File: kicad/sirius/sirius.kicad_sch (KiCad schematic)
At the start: 58 parts, among them J1 IPEX_MHF1, J2 Power In, J3 Screw_Terminal, Q1 Q_PMOS_GSD, Q2 Q_NMOS_GSD, Q3 Q_NMOS_GSD, U1 Power_Connector, U2 AP63301WU-7, U3 RFM95W-915S2, U4 LC29H (DA), U5 Pi Zero 2W

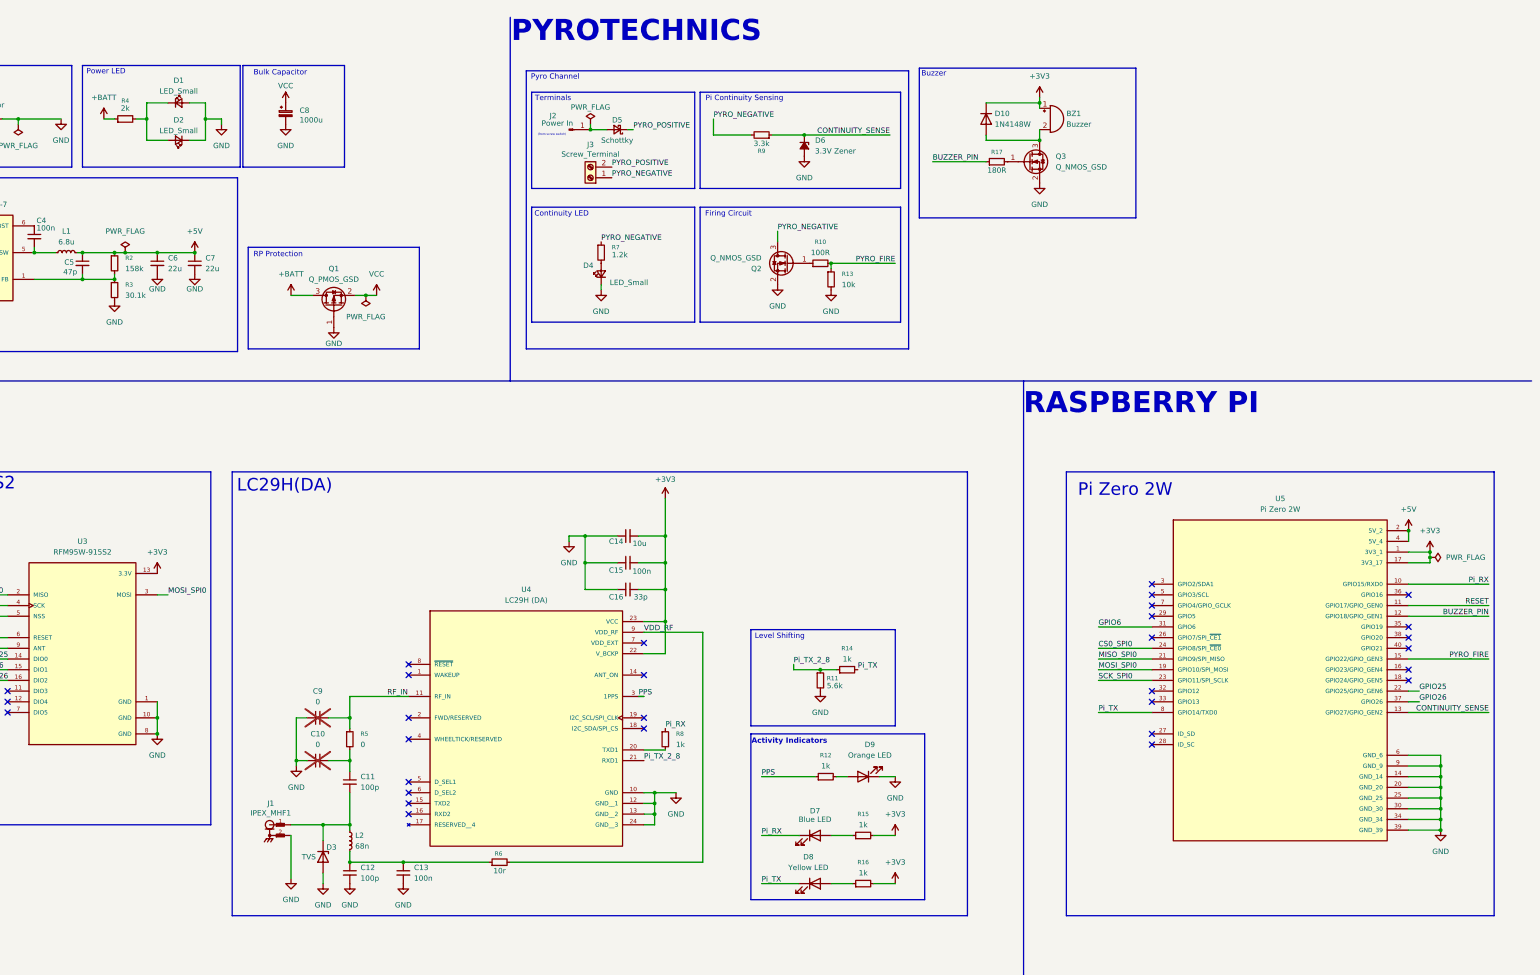
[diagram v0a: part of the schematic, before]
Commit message: WIP: Start making new version of Sirius
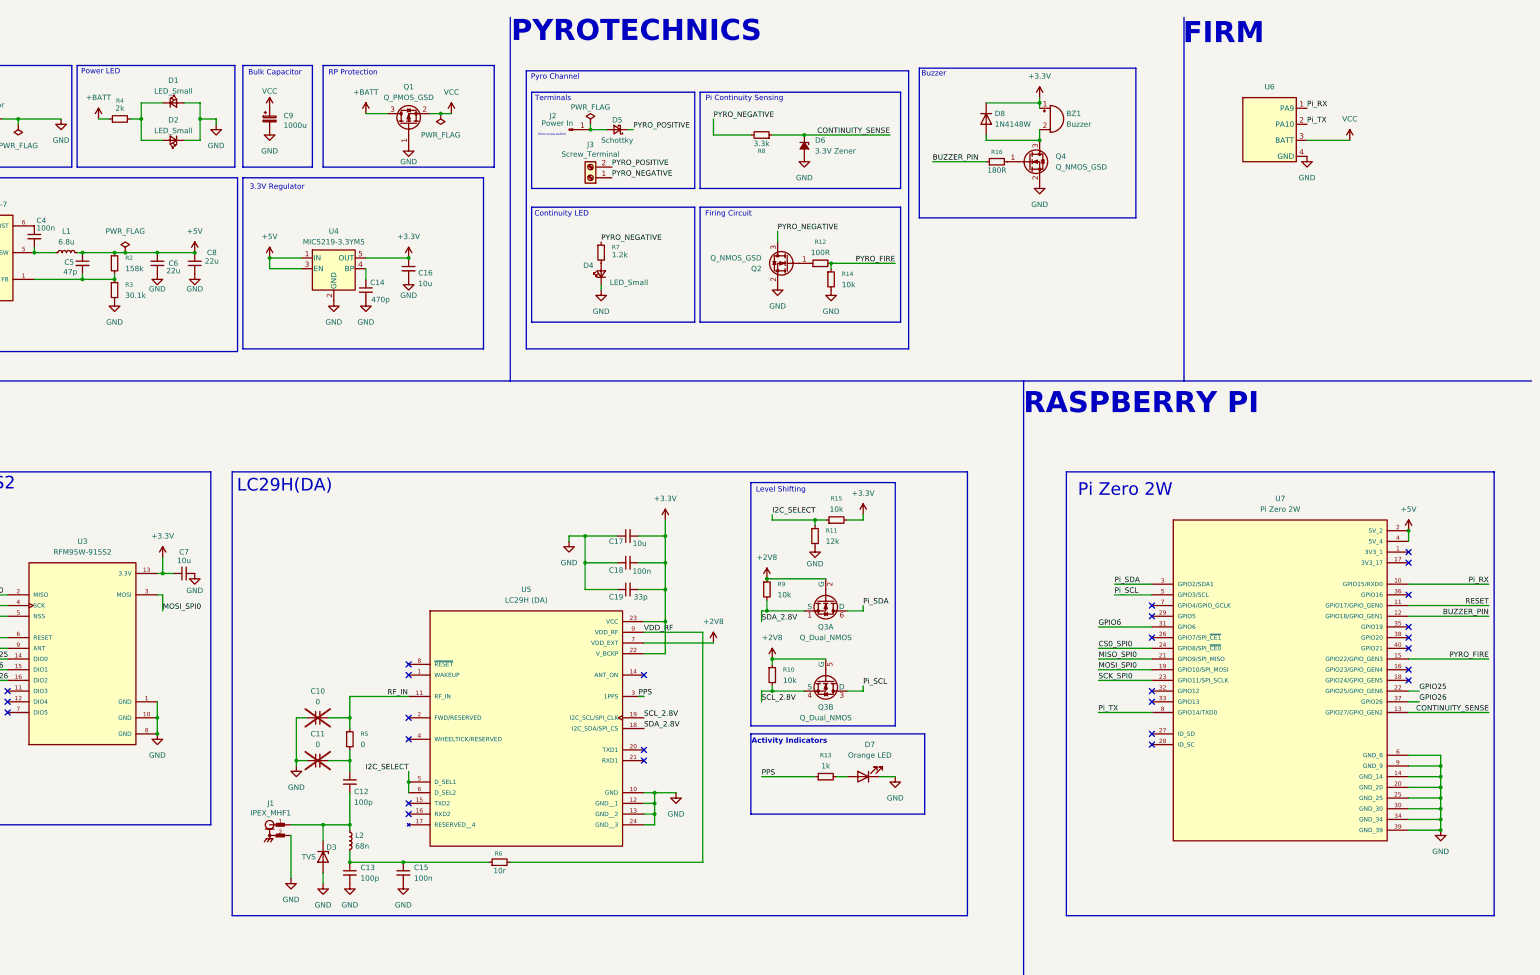
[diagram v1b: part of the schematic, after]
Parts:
- removed D7: Blue LED, LED_SMD:LED_0603_1608Metric_Pad1.05x0.95mm_HandSolder, symbol Device:LED
- removed D8: Yellow LED, LED_SMD:LED_0603_1608Metric_Pad1.05x0.95mm_HandSolder, symbol Device:LED
- removed R14, R8: 1k, Resistor_SMD:R_0603_1608Metric_Pad0.98x0.95mm_HandSolder, symbol Device:R_Small
- removed R16: 1k, Resistor_SMD:R_0603_1608Metric, symbol Device:R_Small
- added C14: 470p, Capacitor_SMD:C_0603_1608Metric, symbol Device:C_Small
- added C16: 10u, Capacitor_SMD:C_0603_1608Metric, symbol Device:C_Small
- added C8: 22u, Capacitor_SMD:C_0603_1608Metric, symbol Device:C_Small
- added Q3: Q_Dual_NMOS, Package_TO_SOT_SMD:SOT-363_SC-70-6, symbol Transistor_FET:Q_Dual_NMOS_S1G1D2S2G2D1
- added R10, R9: 10k, Resistor_SMD:R_0603_1608Metric, symbol Device:R_Small
- added U4: MIC5219-3.3YM5, Package_TO_SOT_SMD:SOT-23-5, symbol Regulator_Linear:MIC5219-3.3YM5
- added U6: (no value), sirius:FIRM v1.0, symbol sirius:FIRM v1.0
- C1, C4, C5: footprint Capacitor_SMD:C_0603_1608Metric_Pad1.08x0.95mm_HandSolder -> Capacitor_SMD:C_0603_1608Metric
- C10: renamed from C9; footprint Capacitor_SMD:C_0603_1608Metric -> Capacitor_SMD:C_0402_1005Metric_Pad0.74x0.62mm_HandSolder
- C11: renamed from C10; footprint Capacitor_SMD:C_0603_1608Metric -> Capacitor_SMD:C_0402_1005Metric_Pad0.74x0.62mm_HandSolder
- C12: renamed from C11; footprint Capacitor_SMD:C_0603_1608Metric -> Capacitor_SMD:C_0402_1005Metric_Pad0.74x0.62mm_HandSolder; Digikey PN 490-1427-1-ND -> (none)
- C13: renamed from C12; footprint Capacitor_SMD:C_0603_1608Metric -> Capacitor_SMD:C_0402_1005Metric_Pad0.74x0.62mm_HandSolder; Digikey PN 490-1427-1-ND -> (none)
- C15: renamed from C13; footprint Capacitor_SMD:C_0603_1608Metric -> Capacitor_SMD:C_0402_1005Metric_Pad0.74x0.62mm_HandSolder; Digikey PN 399-C0603C104K3RACTUCT-ND -> (none)
- C6: footprint Capacitor_SMD:C_1206_3216Metric -> Capacitor_SMD:C_0603_1608Metric; Digikey PN 587-3246-1-ND -> (none)
- C7: value 22u -> 10u; footprint Capacitor_SMD:C_1206_3216Metric -> Capacitor_SMD:C_0603_1608Metric; Digikey PN 587-3246-1-ND -> 587-3258-1-ND
- J2: footprint Connector_PinHeader_1.00mm:PinHeader_1x01_P1.00mm_Vertical -> Connector_PinHeader_2.54mm:PinHeader_1x01_P2.54mm_Vertical
- J3: footprint sirius:CUI_TB002-500-02BE -> Connector_PinHeader_2.54mm:PinHeader_1x02_P2.54mm_Vertical; Digikey PN 102-6145-ND -> (none); now left out of the parts list
- L2: footprint Inductor_SMD:L_0603_1608Metric -> Inductor_SMD:L_0402_1005Metric_Pad0.77x0.64mm_HandSolder; Digikey PN 490-1178-1-ND -> (none)
- R11: value 5.6k -> 12k; footprint Resistor_SMD:R_0603_1608Metric_Pad0.98x0.95mm_HandSolder -> Resistor_SMD:R_0603_1608Metric; Digikey PN 311-5.60KHRCT-ND -> (none)
- R12: renamed from R10; footprint Resistor_SMD:R_0603_1608Metric_Pad0.98x0.95mm_HandSolder -> Resistor_SMD:R_0603_1608Metric
- R14: renamed from R13; footprint Resistor_SMD:R_0603_1608Metric_Pad0.98x0.95mm_HandSolder -> Resistor_SMD:R_0603_1608Metric
- R15: value 1k -> 10k; Digikey PN RMCF0603FT1K00CT-ND -> 311-10.0KHRCT-ND
- R16: renamed from R17; footprint Resistor_SMD:R_0603_1608Metric_Pad0.98x0.95mm_HandSolder -> Resistor_SMD:R_0603_1608Metric
- R2, R3, R4, R7: footprint Resistor_SMD:R_0603_1608Metric_Pad0.98x0.95mm_HandSolder -> Resistor_SMD:R_0603_1608Metric
- R5: footprint Resistor_SMD:R_0603_1608Metric -> Resistor_SMD:R_0402_1005Metric_Pad0.72x0.64mm_HandSolder; Digikey PN 311-0.0GRCT-ND -> (none)
- R6: footprint Resistor_SMD:R_0603_1608Metric -> Resistor_SMD:R_0402_1005Metric_Pad0.72x0.64mm_HandSolder; Digikey PN RMCF0603FT10R0CT-ND -> (none)
- R8: renamed from R9; footprint Resistor_SMD:R_0603_1608Metric_Pad0.98x0.95mm_HandSolder -> Resistor_SMD:R_0603_1608Metric
- renumbered C14 to C17, C15 to C18, C16 to C19, C8 to C9, D9 to D7, D10 to D8, Q3 to Q4, R12 to R13, U4 to U5, U5 to U7
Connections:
- net +5V: now also C6.2, C8.2, U4.1 (IN), U4.3 (EN); no longer C6.1, C7.1
- net GND: now also C6.1, C14.2, C16.2, C8.1, U4.2 (GND), U6.4 (GND); no longer C6.2
- net Pi_RX: now also U6.1 (PA9)
- net Pi_TX: now also U6.2 (PA10)
- net VCC: now also U6.3 (BATT)
- net I2C_SELECT: now reaches R15.1
- net I2C_SELECT: now also R11.1, U5.5 (D_SEL1), U5.6 (D_SEL2)
- net SDA_2.8V: now reaches U5.18 (I2C_SDA/SPI_CS)
- net SDA_2.8V: now also Q3.1 (S), R9.2
- net SCL_2.8V: now reaches U5.19 (I2C_SCL/SPI_CLK)
- net SCL_2.8V: now also Q3.4 (S), R10.2
- net +2V8: now reaches U5.7 (VDD_EXT)
- net +2V8: now also Q3.2 (G), Q3.5 (G), R10.1, R9.1
- net Pi_SDA: now reaches U7.3 (GPIO2/SDA1)
- net Pi_SDA: now also Q3.6 (D)
- net Pi_SCL: now reaches U7.5 (GPIO3/SCL)
- net Pi_SCL: now also Q3.3 (D)
- net +3V3 renamed +3.3V
- net +3.3V: now also C7.1, C16.1, U4.5 (OUT); no longer U7.1 (3V3_1), U7.17 (3V3_17)
- net Pi_TX_2_8: no longer names the net of U5.21 (RXD1)
- net Pi_TX_2_8: no longer R11.1
- new net: C14.1, U4.4 (BP)
- no-connect marks 30 -> 27
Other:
- note added: "3.3V Regulator"
- note added: "FIRM"
- moved on the sheet: C9, D1, D2, Q1, R4

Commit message: Finish Sirius v0.2
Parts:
- C12, C13: Digikey PN (none) -> 399-C0402C101J5GACTUCT-ND
- C14: Digikey PN (none) -> 1276-1168-1-ND
- C15: Digikey PN (none) -> 1276-1002-1-ND
- C16: Digikey PN (none) -> 587-3258-1-ND
- C6, C8: Digikey PN (none) -> 490-GRM188R60J226MEA0JCT-ND
- L2: Digikey PN (none) -> 553-BSCH0010050568NJCPCT-ND
- Q3: Digikey PN (none) -> 31-BSS138DWK-13CT-ND
- R10, R9: Digikey PN (none) -> 311-10.0KHRCT-ND
- R11: Digikey PN (none) -> P12KDBCT-ND
- R5: Digikey PN (none) -> 311-0.0JRCT-ND
- R6: Digikey PN (none) -> 541-10.0LCT-ND
- U7: now left out of the parts list
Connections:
- net RESET: now also U7.7 (GPIO4/GPIO_GCLK); no longer U7.11 (GPIO17/GPIO_GEN0)
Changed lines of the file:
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@@
 	)
 	(no_connect
-		(at 314.96 153.67)
+		(at 43.18 173.99)
 	)
 	(no_connect
-		(at 43.18 173.99)
+		(at 375.92 153.67)
 	)
 	(no_connect
@@
 	(wire
 		(pts
-			(xy 394.97 153.67) (xy 375.92 153.67)
-		)
-		(stroke
-			(width 0)
-			(type default)
-		)
-	)
-	(wire
-		(pts
 			(xy 181.61 39.37) (xy 181.61 40.64)
 		)
@@
 	(wire
 		(pts
+			(xy 306.07 153.67) (xy 314.96 153.67)
+		)
+		(stroke
+			(width 0)
+			(type default)
+		)
+	)
+	(wire
+		(pts
 			(xy 110.49 205.74) (xy 118.11 205.74)
 		)
@@
 		)
 	)
+	(label "RESET"
+		(at 306.07 153.67 0)
+		(effects
+			(font
+				(size 1.27 1.27)
+			)
+			(justify left bottom)
+		)
+	)
 	(label "PPS"
 		(at 222.25 194.31 0)
@@
 		)
 	)
-	(label "RESET"
-		(at 394.97 153.67 180)
-		(effects
-			(font
-				(size 1.27 1.27)
-			)
-			(justify right bottom)
-		)
-	)
 	(symbol
 		(lib_id "sirius:RFM95W-915S2")
@@
 			)
 		)
-		(property "Digikey PN" ""
+		(property "Digikey PN" "399-C0402C101J5GACTUCT-ND"
 			(at 124.46 217.17 0)
 			(hide yes)
@@
 			)
 		)
-		(property "Datasheet" ""
+		(property "Datasheet" "https://www.diodes.com/assets/Datasheets/BSS138DWK.pdf"
 			(at 237.49 176.53 0)
 			(hide yes)
@@
 			)
 		)
+		(property "Digikey PN" "31-BSS138DWK-13CT-ND"
+			(at 237.49 171.45 90)
+			(hide yes)
+			(show_name no)
+			(do_not_autoplace no)
+			(effects
+				(font
+					(size 1.27 1.27)
+				)
+			)
+		)
 		(pin "3"
 		)
@@
 			)
 		)
-		(property "Datasheet" ""
+		(property "Datasheet" "https://www.diodes.com/assets/Datasheets/BSS138DWK.pdf"
 			(at 237.49 157.48 0)
 			(hide yes)
@@
 			)
 		)
+		(property "Digikey PN" "31-BSS138DWK-13CT-ND"
+			(at 237.49 152.4 90)
+			(hide yes)
+			(show_name no)
+			(do_not_autoplace no)
+			(effects
+				(font
+					(size 1.27 1.27)
+				)
+			)
+		)
 		(pin "3"
 		)
@@
 			)
 		)
-		(property "Digikey PN" ""
+		(property "Digikey PN" "553-BSCH0010050568NJCPCT-ND"
 			(at 124.46 209.55 0)
 			(hide yes)
@@
 			)
 		)
+		(property "Digikey PN" "P12KDBCT-ND"
+			(at 234.95 137.16 0)
+			(hide yes)
+			(show_name no)
+			(do_not_autoplace no)
+			(effects
+				(font
+					(size 1.27 1.27)
+				)
+			)
+		)
 		(pin "1"
 		)
@@
 			)
 		)
+		(property "Digikey PN" "587-3258-1-ND"
+			(at 138.43 73.66 0)
+			(hide yes)
+			(show_name no)
+			(do_not_autoplace no)
+			(effects
+				(font
+					(size 1.27 1.27)
+				)
+			)
+		)
 		(pin "1"
 		)
@@
 			)
 		)
+		(property "Digikey PN" "311-10.0KHRCT-ND"
+			(at 223.52 149.86 0)
+			(hide yes)
+			(show_name no)
+			(do_not_autoplace no)
+			(effects
+				(font
+					(size 1.27 1.27)
+				)
+			)
+		)
 		(pin "1"
 		)
@@
 			)
 		)
+		(property "Digikey PN" "311-10.0KHRCT-ND"
+			(at 224.79 170.18 0)
+			(hide yes)
+			(show_name no)
+			(do_not_autoplace no)
+			(effects
+				(font
+					(size 1.27 1.27)
+				)
+			)
+		)
 		(pin "2"
 		)
@@
 			)
 		)
-		(property "Digikey PN" ""
+		(property "Digikey PN" "490-GRM188R60J226MEA0JCT-ND"
 			(at 78.74 72.39 90)
 			(hide yes)
@@
 			)
 		)
-		(property "Digikey PN" ""
+		(property "Digikey PN" "1276-1002-1-ND"
 			(at 137.16 217.17 0)
 			(hide yes)
@@
 			)
 		)
-		(property "Digikey PN" ""
+		(property "Digikey PN" "490-GRM188R60J226MEA0JCT-ND"
 			(at 87.63 72.39 90)
 			(hide yes)
@@
 			)
 		)
-		(property "Digikey PN" ""
+		(property "Digikey PN" "399-C0402C101J5GACTUCT-ND"
 			(at 124.46 195.58 0)
 			(hide yes)
@@
 			)
 		)
-		(property "Digikey PN" ""
+		(property "Digikey PN" "541-10.0LCT-ND"
 			(at 160.02 214.63 90)
 			(hide yes)
@@
 			)
 		)
-		(property "Digikey PN" ""
+		(property "Digikey PN" "311-0.0JRCT-ND"
 			(at 124.46 185.42 0)
 			(hide yes)
@@
 			)
 		)
+		(property "Digikey PN" "1276-1168-1-ND"
+			(at 128.27 78.74 0)
+			(hide yes)
+			(show_name no)
+			(do_not_autoplace no)
+			(effects
+				(font
+					(size 1.27 1.27)
+				)
+			)
+		)
 		(pin "2"
 		)
@@
 		(body_style 1)
 		(exclude_from_sim no)
-		(in_bom yes)
+		(in_bom no)
 		(on_board yes)
 		(in_pos_files yes)
